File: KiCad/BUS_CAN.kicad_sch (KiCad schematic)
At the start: 4 parts, among them J3 DE9_Pins_MountingHoles

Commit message: Errors solucionats
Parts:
- added J1: DE9_Pins_MountingHoles, Connector_Dsub:DSUB-9_Socket_Vertical_P2.77x2.84mm_MountingHoles, symbol Connector:DE9_Pins_MountingHoles
- added U2: SN65HVD230, Package_SO:SOIC-8_3.9x4.9mm_P1.27mm, symbol Interface_CAN_LIN:SN65HVD230
- renumbered C8 to C1, J3 to J2
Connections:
- net +3.3V: now also U2.3 (VCC)
- net CANH: now also J1.7, U2.7 (CANH)
- net CANL: now also J1.2, U2.6 (CANL)
- net CAN_RX: now also U2.4 (R)
- net CAN_TX: now also U2.1 (D)
- net GND: now also C1.1, J2.5, J1.3, J1.6, U2.2 (GND)
- net at R2.1: now also U2.8 (Rs)
- no-connect marks 13 -> 14

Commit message: V2 placement
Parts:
- J1, J2: footprint Connector_Dsub:DSUB-9_Socket_Vertical_P2.77x2.84mm_MountingHoles -> Connector_Dsub:DSUB-15_Socket_Horizontal_P2.77x2.84mm_EdgePinOffset4.94mm_Housed_MountingHolesOffset4.94mm
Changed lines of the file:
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@@
+				)
+			)
+			(project "BUS_CAN"
+				(path "/d214e8f9-d2e5-4815-9ff0-dfe8e2320eb5"
+					(reference "#PWR0101")
+					(unit 1)
 				)
 			)
@@
 				)
 			)
+			(project "BUS_CAN"
+				(path "/d214e8f9-d2e5-4815-9ff0-dfe8e2320eb5"
+					(reference "#PWR0102")
+					(unit 1)
+				)
+			)
 		)
 	)
@@
 				)
 			)
+			(project "BUS_CAN"
+				(path "/d214e8f9-d2e5-4815-9ff0-dfe8e2320eb5"
+					(reference "U1")
+					(unit 1)
+				)
+			)
 		)
 	)
@@
 				)
 			)
+			(project "BUS_CAN"
+				(path "/d214e8f9-d2e5-4815-9ff0-dfe8e2320eb5"
+					(reference "#PWR0105")
+					(unit 1)
+				)
+			)
 		)
 	)
@@
 				)
 			)
+			(project "BUS_CAN"
+				(path "/d214e8f9-d2e5-4815-9ff0-dfe8e2320eb5"
+					(reference "R1")
+					(unit 1)
+				)
+			)
 		)
 	)
@@
 				)
 			)
+			(project "BUS_CAN"
+				(path "/d214e8f9-d2e5-4815-9ff0-dfe8e2320eb5"
+					(reference "#PWR0106")
+					(unit 1)
+				)
+			)
 		)
 	)
@@
 			)
 		)
-		(property "Footprint" "Connector_Dsub:DSUB-9_Socket_Vertical_P2.77x2.84mm_MountingHoles"
+		(property "Footprint" "Connector_Dsub:DSUB-15_Socket_Horizontal_P2.77x2.84mm_EdgePinOffset4.94mm_Housed_MountingHolesOffset4.94mm"
 			(at 195.58 52.07 0)
 			(effects
@@
 			(project "PROJECTE_EINES"
 				(path "/347831db-5db9-4aff-ad32-e56fd770e219/119ce145-2c93-4544-b106-e85ec51fdc64"
+					(reference "J2")
+					(unit 1)
+				)
+			)
+			(project "BUS_CAN"
+				(path "/d214e8f9-d2e5-4815-9ff0-dfe8e2320eb5"
 					(reference "J2")
 					(unit 1)
@@
 				)
 			)
+			(project "BUS_CAN"
+				(path "/d214e8f9-d2e5-4815-9ff0-dfe8e2320eb5"
+					(reference "C1")
+					(unit 1)
+				)
+			)
 		)
 	)
@@
 				)
 			)
+			(project "BUS_CAN"
+				(path "/d214e8f9-d2e5-4815-9ff0-dfe8e2320eb5"
+					(reference "R2")
+					(unit 1)
+				)
+			)
 		)
 	)
@@
 			)
 		)
-		(property "Footprint" "Connector_Dsub:DSUB-9_Socket_Vertical_P2.77x2.84mm_MountingHoles"
+		(property "Footprint" "Connector_Dsub:DSUB-15_Socket_Horizontal_P2.77x2.84mm_EdgePinOffset4.94mm_Housed_MountingHolesOffset4.94mm"
 			(at 125.73 55.88 0)
 			(effects
@@
 			(project "PROJECTE_EINES"
 				(path "/347831db-5db9-4aff-ad32-e56fd770e219/119ce145-2c93-4544-b106-e85ec51fdc64"
+					(reference "J1")
+					(unit 1)
+				)
+			)
+			(project "BUS_CAN"
+				(path "/d214e8f9-d2e5-4815-9ff0-dfe8e2320eb5"
 					(reference "J1")
 					(unit 1)
@@
 				)
 			)
+			(project "BUS_CAN"
+				(path "/d214e8f9-d2e5-4815-9ff0-dfe8e2320eb5"
+					(reference "#PWR0103")
+					(unit 1)
+				)
+			)
 		)
 	)
@@
 				)
 			)
-		)
-	)
+			(project "BUS_CAN"
+				(path "/d214e8f9-d2e5-4815-9ff0-dfe8e2320eb5"
+					(reference "#PWR0104")
+					(unit 1)
+				)
+			)
+		)
+	)
+	(sheet_instances
+		(path "/"
+			(page "1")
+		)
+	)
+	(embedded_fonts no)
 )

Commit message: V1 Routing
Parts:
- J1, J2: footprint Connector_Dsub:DSUB-15_Socket_Horizontal_P2.77x2.84mm_EdgePinOffset4.94mm_Housed_MountingHolesOffset4.94mm -> Connector_Dsub:DSUB-9_Pins_Horizontal_P2.77x2.84mm_EdgePinOffset4.94mm_Housed_MountingHolesOffset4.94mm
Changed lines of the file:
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@@
 		(dnp no)
 		(fields_autoplaced yes)
-		(property "Reference" "#PWR017"
+		(property "Reference" "#PWR019"
 			(at 177.8 49.53 0)
 			(effects
@@
 			(project "PROJECTE_EINES"
 				(path "/347831db-5db9-4aff-ad32-e56fd770e219/119ce145-2c93-4544-b106-e85ec51fdc64"
-					(reference "#PWR017")
-					(unit 1)
-				)
-			)
-			(project "BUS_CAN"
-				(path "/d214e8f9-d2e5-4815-9ff0-dfe8e2320eb5"
-					(reference "#PWR0101")
+					(reference "#PWR019")
 					(unit 1)
 				)
@@
 		(dnp no)
 		(fields_autoplaced yes)
-		(property "Reference" "#PWR012"
+		(property "Reference" "#PWR014"
 			(at 55.88 68.58 0)
 			(effects
@@
 			(project "PROJECTE_EINES"
 				(path "/347831db-5db9-4aff-ad32-e56fd770e219/119ce145-2c93-4544-b106-e85ec51fdc64"
-					(reference "#PWR012")
-					(unit 1)
-				)
-			)
-			(project "BUS_CAN"
-				(path "/d214e8f9-d2e5-4815-9ff0-dfe8e2320eb5"
-					(reference "#PWR0102")
+					(reference "#PWR014")
 					(unit 1)
 				)
@@
 				)
 			)
-			(project "BUS_CAN"
-				(path "/d214e8f9-d2e5-4815-9ff0-dfe8e2320eb5"
-					(reference "U1")
-					(unit 1)
-				)
-			)
 		)
 	)
@@
 		(dnp no)
 		(fields_autoplaced yes)
-		(property "Reference" "#PWR015"
+		(property "Reference" "#PWR017"
 			(at 85.09 81.28 0)
 			(effects
@@
 			(project ""
 				(path "/347831db-5db9-4aff-ad32-e56fd770e219/119ce145-2c93-4544-b106-e85ec51fdc64"
-					(reference "#PWR015")
-					(unit 1)
-				)
-			)
-			(project "BUS_CAN"
-				(path "/d214e8f9-d2e5-4815-9ff0-dfe8e2320eb5"
-					(reference "#PWR0105")
+					(reference "#PWR017")
 					(unit 1)
 				)
@@
 				)
 			)
-			(project "BUS_CAN"
-				(path "/d214e8f9-d2e5-4815-9ff0-dfe8e2320eb5"
-					(reference "R1")
-					(unit 1)
-				)
-			)
 		)
 	)
@@
 		(on_board yes)
 		(dnp no)
-		(property "Reference" "#PWR016"
+		(property "Reference" "#PWR018"
 			(at 111.76 62.23 0)
 			(effects
@@
 			(project "PROJECTE_EINES"
 				(path "/347831db-5db9-4aff-ad32-e56fd770e219/119ce145-2c93-4544-b106-e85ec51fdc64"
-					(reference "#PWR016")
-					(unit 1)
-				)
-			)
-			(project "BUS_CAN"
-				(path "/d214e8f9-d2e5-4815-9ff0-dfe8e2320eb5"
-					(reference "#PWR0106")
+					(reference "#PWR018")
 					(unit 1)
 				)
@@
 			)
 		)
-		(property "Footprint" "Connector_Dsub:DSUB-15_Socket_Horizontal_P2.77x2.84mm_EdgePinOffset4.94mm_Housed_MountingHolesOffset4.94mm"
+		(property "Footprint" "Connector_Dsub:DSUB-9_Pins_Horizontal_P2.77x2.84mm_EdgePinOffset4.94mm_Housed_MountingHolesOffset4.94mm"
 			(at 195.58 52.07 0)
 			(effects
@@
 			(project "PROJECTE_EINES"
 				(path "/347831db-5db9-4aff-ad32-e56fd770e219/119ce145-2c93-4544-b106-e85ec51fdc64"
-					(reference "J2")
-					(unit 1)
-				)
-			)
-			(project "BUS_CAN"
-				(path "/d214e8f9-d2e5-4815-9ff0-dfe8e2320eb5"
 					(reference "J2")
 					(unit 1)
@@
 				)
 			)
-			(project "BUS_CAN"
-				(path "/d214e8f9-d2e5-4815-9ff0-dfe8e2320eb5"
-					(reference "C1")
-					(unit 1)
-				)
-			)
 		)
 	)
@@
 				)
 			)
-			(project "BUS_CAN"
-				(path "/d214e8f9-d2e5-4815-9ff0-dfe8e2320eb5"
-					(reference "R2")
-					(unit 1)
-				)
-			)
 		)
 	)
@@
 			)
 		)
-		(property "Footprint" "Connector_Dsub:DSUB-15_Socket_Horizontal_P2.77x2.84mm_EdgePinOffset4.94mm_Housed_MountingHolesOffset4.94mm"
+		(property "Footprint" "Connector_Dsub:DSUB-9_Pins_Horizontal_P2.77x2.84mm_EdgePinOffset4.94mm_Housed_MountingHolesOffset4.94mm"
 			(at 125.73 55.88 0)
 			(effects
@@
 				)
 			)
-			(project "BUS_CAN"
-				(path "/d214e8f9-d2e5-4815-9ff0-dfe8e2320eb5"
-					(reference "J1")
-					(unit 1)
-				)
-			)
 		)
 	)
@@
 		(dnp no)
 		(fields_autoplaced yes)
-		(property "Reference" "#PWR014"
+		(property "Reference" "#PWR016"
 			(at 85.09 41.91 0)
 			(effects
@@
 			(project ""
 				(path "/347831db-5db9-4aff-ad32-e56fd770e219/119ce145-2c93-4544-b106-e85ec51fdc64"
-					(reference "#PWR014")
-					(unit 1)
-				)
-			)
-			(project "BUS_CAN"
-				(path "/d214e8f9-d2e5-4815-9ff0-dfe8e2320eb5"
-					(reference "#PWR0103")
+					(reference "#PWR016")
 					(unit 1)
 				)
@@
 		(dnp no)
 		(fields_autoplaced yes)
-		(property "Reference" "#PWR013"
+		(property "Reference" "#PWR015"
 			(at 63.5 50.8 0)
 			(effects
@@
 			(project "PROJECTE_EINES"
 				(path "/347831db-5db9-4aff-ad32-e56fd770e219/119ce145-2c93-4544-b106-e85ec51fdc64"
-					(reference "#PWR013")
-					(unit 1)
-				)
-			)
-			(project "BUS_CAN"
-				(path "/d214e8f9-d2e5-4815-9ff0-dfe8e2320eb5"
-					(reference "#PWR0104")
-					(unit 1)
-				)
-			)
-		)
-	)
-	(sheet_instances
-		(path "/"
-			(page "1")
-		)
-	)
-	(embedded_fonts no)
+					(reference "#PWR015")
+					(unit 1)
+				)
+			)
+		)
+	)
 )

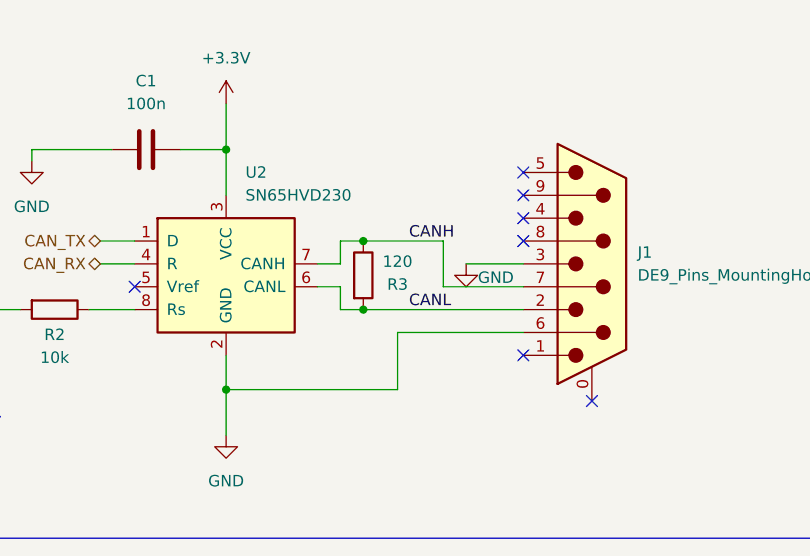
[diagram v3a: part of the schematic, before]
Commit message: Actualització dels test points
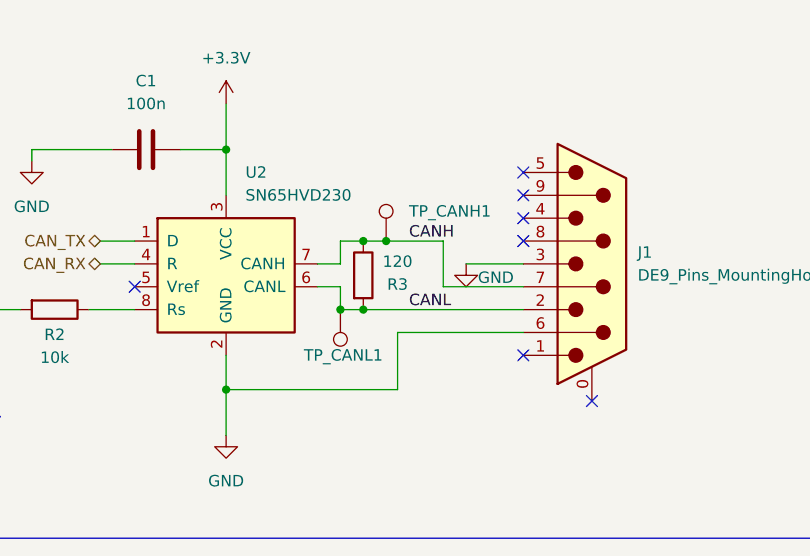
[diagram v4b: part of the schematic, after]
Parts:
- added TP_CANH1, TP_CANL1: ~, TestPoint:TestPoint_Pad_D1.5mm, symbol Connector:TestPoint
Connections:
- net CANH: now also TP_CANH1.1
- net CANL: now also TP_CANL1.1
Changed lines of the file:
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@@
+	)
+	(junction
+		(at 102.87 53.34)
+		(diameter 0)
+		(color 0 0 0 0)
 	)
 	(junction
@@
 	)
 	(junction
+		(at 97.79 60.96)
+		(diameter 0)
+		(color 0 0 0 0)
+	)
+	(junction
 		(at 85.09 69.85)
 		(diameter 0)
@@
 	(wire
 		(pts
-			(xy 100.33 53.34) (xy 109.22 53.34)
+			(xy 100.33 53.34) (xy 102.87 53.34)
 		)
 		(stroke
@@
 		(pts
 			(xy 100.33 60.96) (xy 118.11 60.96)
+		)
+		(stroke
+			(width 0)
+			(type default)
+		)
+	)
+	(wire
+		(pts
+			(xy 102.87 53.34) (xy 109.22 53.34)
 		)
 		(stroke
@@
 	)
 	(symbol
+		(lib_id "Connector:TestPoint")
+		(at 97.79 60.96 180)
+		(unit 1)
+		(exclude_from_sim no)
+		(in_bom yes)
+		(on_board yes)
+		(dnp no)
+		(property "Reference" "TP_CANL1"
+			(at 93.726 66.04 0)
+			(effects
+				(font
+					(size 1.27 1.27)
+				)
+				(justify right)
+			)
+		)
+		(property "Value" "~"
+			(at 95.25 62.9921 0)
+			(effects
+				(font
+					(size 1.27 1.27)
+				)
+				(justify left)
+				(hide yes)
+			)
+		)
+		(property "Footprint" "TestPoint:TestPoint_Pad_D1.5mm"
+			(at 92.71 60.96 0)
+			(effects
+				(font
+					(size 1.27 1.27)
+				)
+				(hide yes)
+			)
+		)
+		(property "Datasheet" "~"
+			(at 92.71 60.96 0)
+			(effects
+				(font
+					(size 1.27 1.27)
+				)
+				(hide yes)
+			)
+		)
+		(property "Description" "test point"
+			(at 97.79 60.96 0)
+			(effects
+				(font
+					(size 1.27 1.27)
+				)
+				(hide yes)
+			)
+		)
+		(pin "1"
+		)
+		(instances
+			(project "PROJECTE_EINES"
+				(path "/347831db-5db9-4aff-ad32-e56fd770e219/119ce145-2c93-4544-b106-e85ec51fdc64"
+					(reference "TP_CANL1")
+					(unit 1)
+				)
+			)
+		)
+	)
+	(symbol
 		(lib_id "Interface_CAN_LIN:SN65HVD230")
 		(at 85.09 55.88 0)
@@
 					(unit 1)
 				)
+			)
+		)
+	)
+	(symbol
+		(lib_id "Connector:TestPoint")
+		(at 102.87 53.34 0)
+		(unit 1)
+		(exclude_from_sim no)
+		(in_bom yes)
+		(on_board yes)
+		(dnp no)
+		(fields_autoplaced yes)
+		(property "Reference" "TP_CANH1"
+			(at 105.41 50.0379 0)
+			(effects
+				(font
+					(size 1.27 1.27)
+				)
+				(justify left)
+			)
+		)
+		(property "Value" "~"
+			(at 105.41 51.3079 0)
+			(effects
+				(font
+					(size 1.27 1.27)
+				)
+				(justify left)
+				(hide yes)
+			)
+		)
+		(property "Footprint" "TestPoint:TestPoint_Pad_D1.5mm"
+			(at 107.95 53.34 0)
+			(effects
+				(font
+					(size 1.27 1.27)
+				)
+				(hide yes)
+			)
+		)
+		(property "Datasheet" "~"
+			(at 107.95 53.34 0)
+			(effects
+				(font
+					(size 1.27 1.27)
+				)
+				(hide yes)
+			)
+		)
+		(property "Description" "test point"
+			(at 102.87 53.34 0)
+			(effects
+				(font
+					(size 1.27 1.27)
+				)
+				(hide yes)
+			)
+		)
+		(pin "1"
+		)
+		(instances
+			(project ""
+				(path "/347831db-5db9-4aff-ad32-e56fd770e219/119ce145-2c93-4544-b106-e85ec51fdc64"
+					(reference "TP_CANH1")
+					(unit 1)
+				)

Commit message: Versió Final projecte
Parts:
- renumbered C1 to C7
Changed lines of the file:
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@@
 		(dnp no)
 		(fields_autoplaced yes)
-		(property "Reference" "C1"
+		(property "Reference" "C7"
 			(at 76.2 35.56 90)
 			(effects
@@
 			(project ""
 				(path "/347831db-5db9-4aff-ad32-e56fd770e219/119ce145-2c93-4544-b106-e85ec51fdc64"
-					(reference "C1")
+					(reference "C7")
 					(unit 1)
 				)
